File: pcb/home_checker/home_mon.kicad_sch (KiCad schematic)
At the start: 16 parts, among them J12 220va, J14 J14, J15 J13, J4 J15, J5 J16, J6 UART, J7 Jumper, J8 T° sensor, J9 Alim, K1 FINDER-40.52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

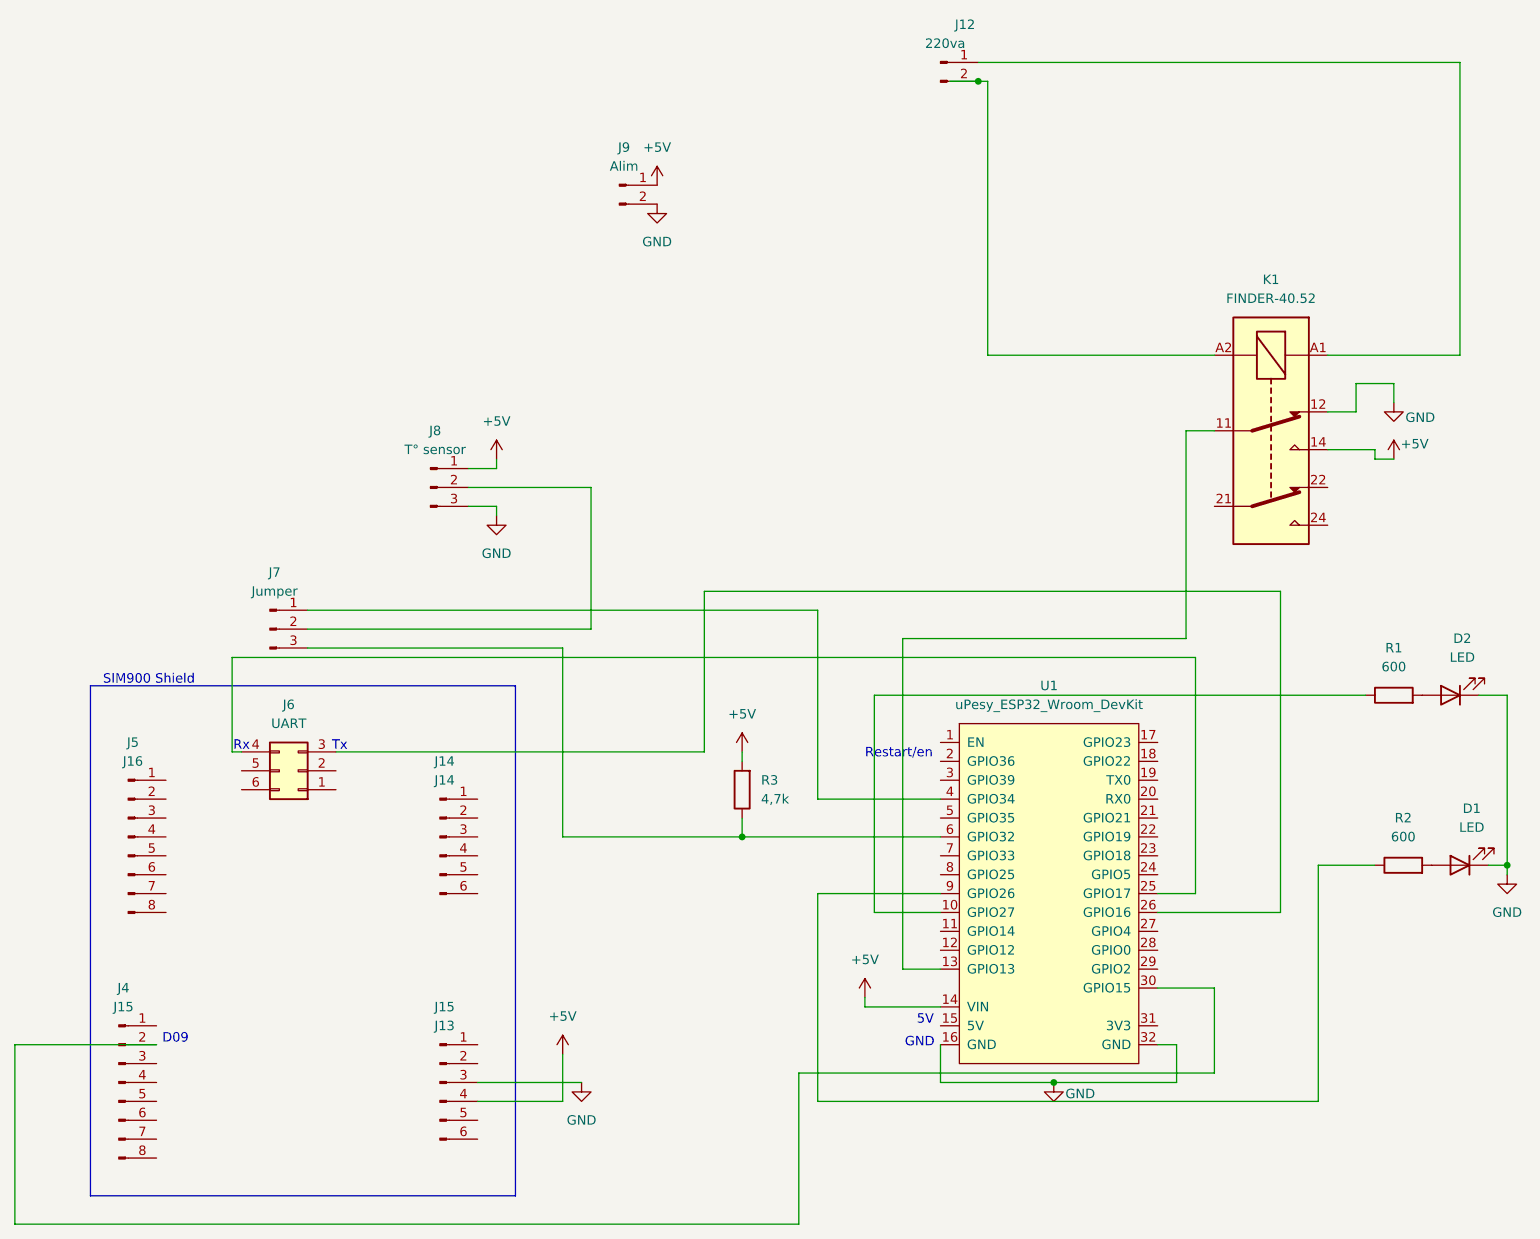
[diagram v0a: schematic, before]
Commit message: feat: Monitor the battery voltage
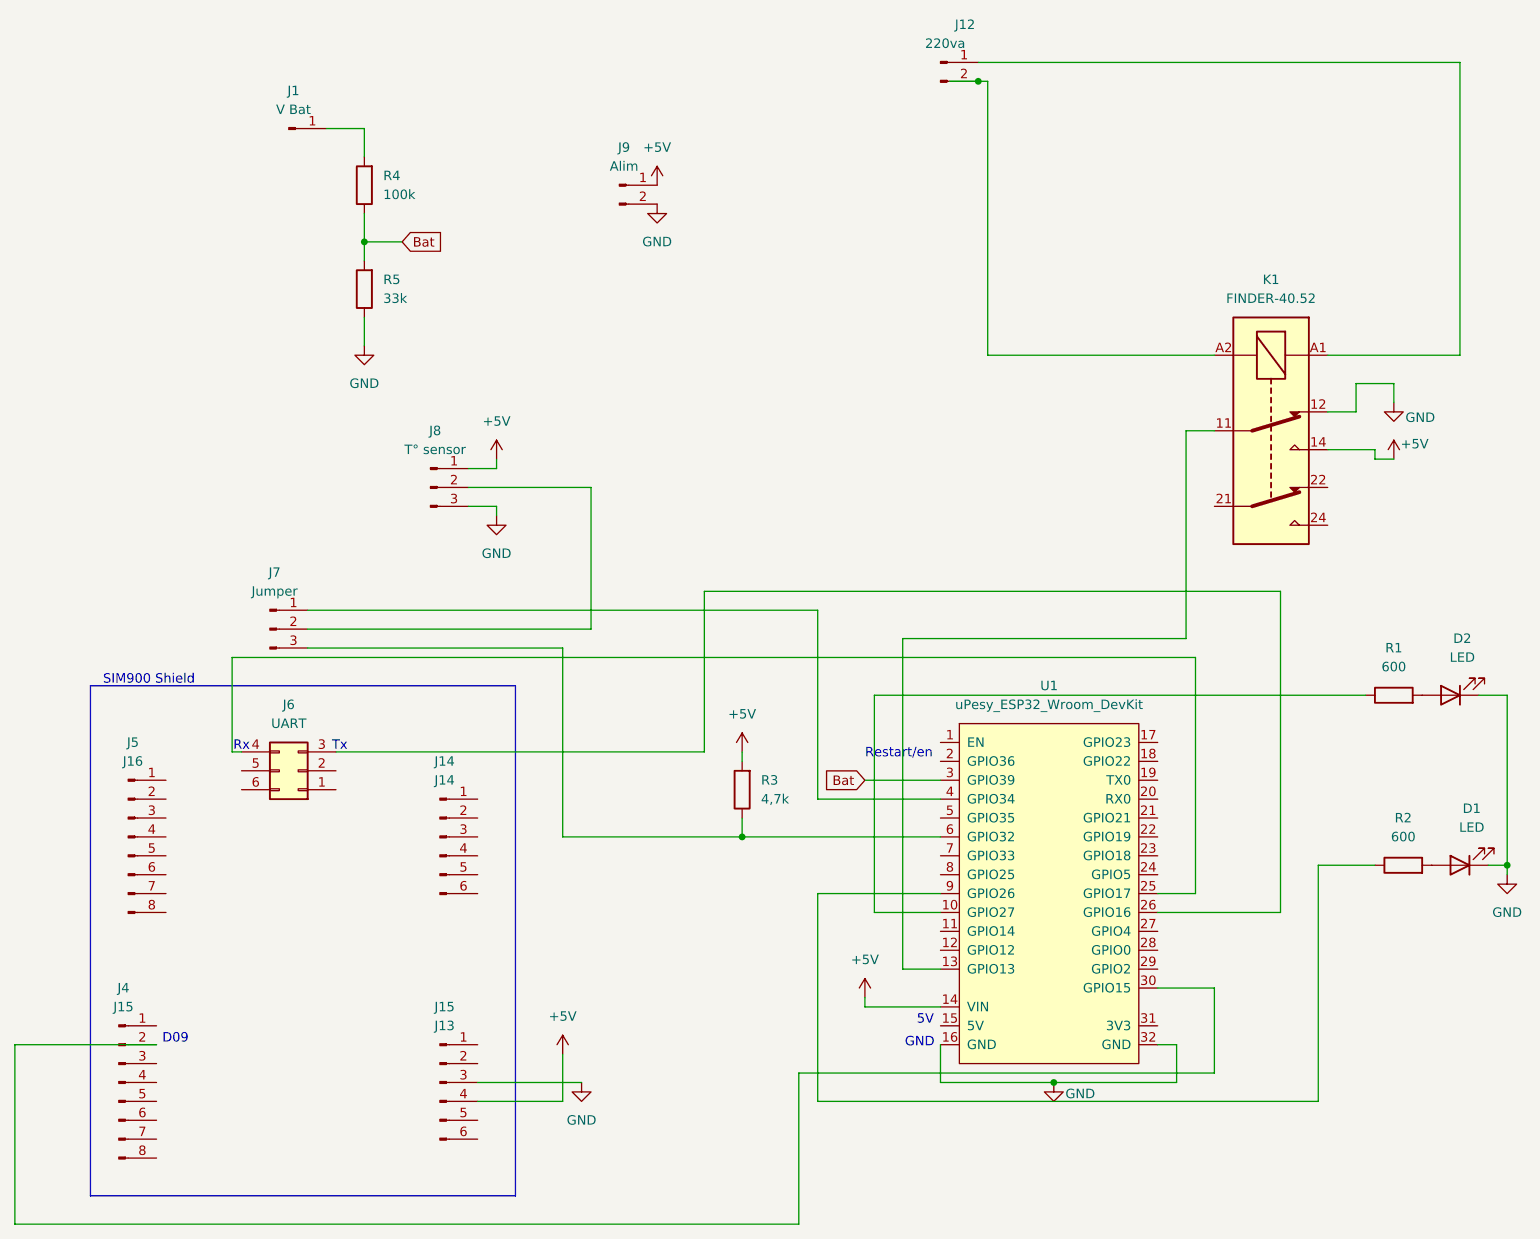
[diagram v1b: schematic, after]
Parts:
- added J1: V Bat, TestPoint:TestPoint_Loop_D1.80mm_Drill1.0mm_Beaded, symbol Connector:Conn_01x01_Pin
- added R4: 100k, Resistor_THT:R_Axial_DIN0207_L6.3mm_D2.5mm_P10.16mm_Horizontal, symbol Device:R
- added R5: 33k, Resistor_THT:R_Axial_DIN0207_L6.3mm_D2.5mm_P10.16mm_Horizontal, symbol Device:R
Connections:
- net GND: now also R5.1
- net Bat: now reaches U1.3 (GPIO39)
- net Bat: now also R4.1, R5.2
- new net: J1.1 (Pin_1), R4.2

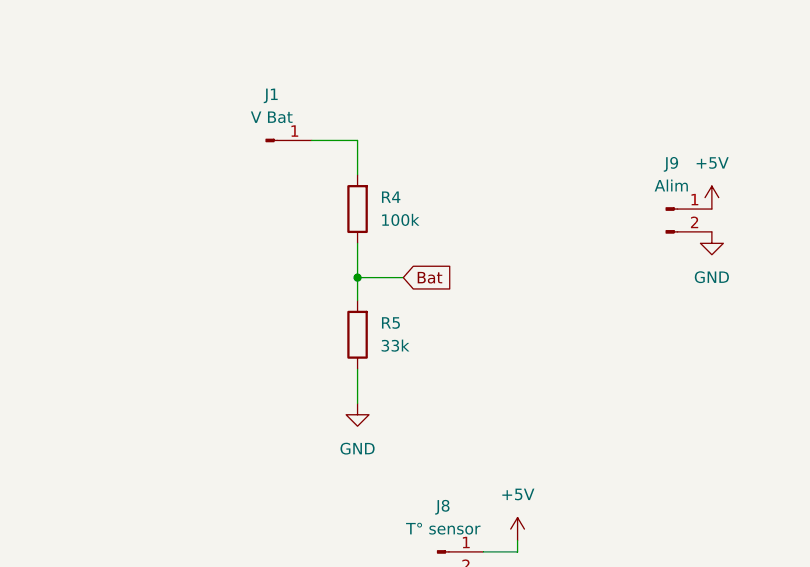
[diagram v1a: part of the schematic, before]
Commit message: fix: Make the sending of sending operational again (canary exception) Make the ADC more reliable
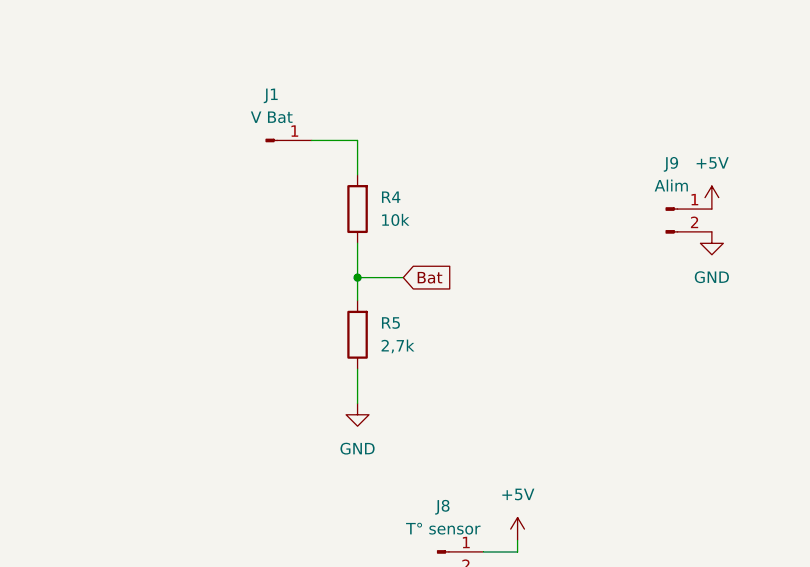
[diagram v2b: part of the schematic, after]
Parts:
- R4: value 100k -> 10k
- R5: value 33k -> 2,7k
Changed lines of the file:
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@@
 			)
 		)
-		(property "Value" "100k"
+		(property "Value" "10k"
 			(at 110.49 43.1799 0)
 			(effects
@@
 			)
 		)
-		(property "Value" "33k"
+		(property "Value" "2,7k"
 			(at 110.49 57.1499 0)
 			(effects
